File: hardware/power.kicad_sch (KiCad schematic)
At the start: 19 parts, among them U1 RY1303

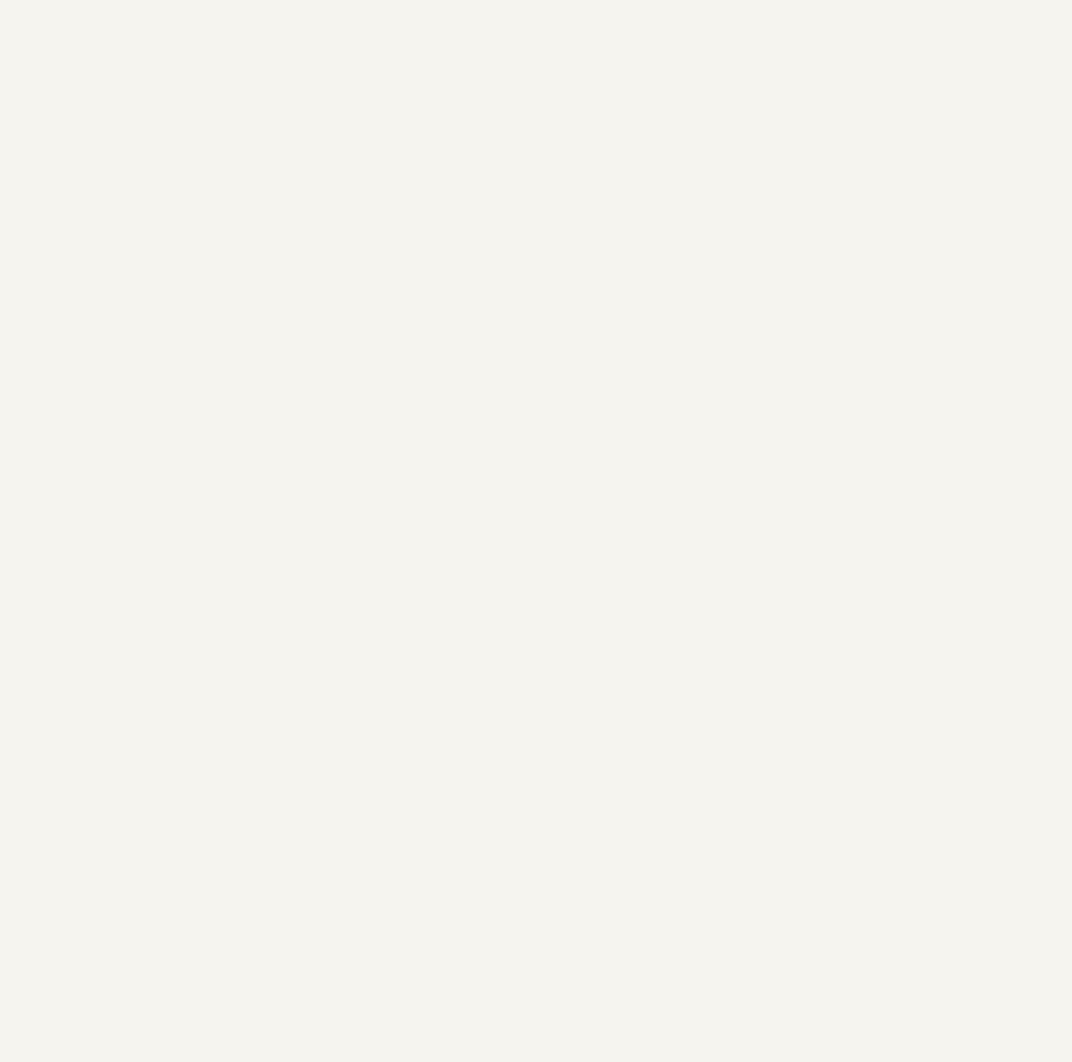
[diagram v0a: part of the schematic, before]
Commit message: 電源頁:兩顆 1.8V LDO 完成
U2/U3 皆用 KiCad 內建 Regulator_Linear:AP2112K-1.8,不必自建符號。
  U2  VIN→+3V3  EN→+3V3  VOUT→+1V8_SOC    Cin=C9   Cout=C11
  U3  VIN→+3V3  EN→+3V3  VOUT→+1V8_HDMI   Cin=C10  Cout=C12
兩顆同料號(011 §3),ADV7511 依 ADI §6.8 需專屬 LDO。

★ U3 一開始整顆接錯,其中兩項會燒件:
  VIN→GND(無輸入)、EN→GND(關閉)、VOUT→+1V8_SOC(接到 U2 的輸出)、C10 兩腳短路。
  第三項最危險:LDO 內部 VOUT→VIN 有寄生二極體(同概念 ⑦ 的 IO 箝位二極體),
  U2 的 1.8V 從 U3 的 VOUT 灌入而其 VIN=0V → 反向偏壓,
  U3 可能燒毀且會拉垮 U2 輸出。

★ 模式:「複製後漏改」連續第二次
  09-29 複製 buck 那路漏改 FB 接點;09-30 複製 LDO 那組漏改 VIN/EN/VOUT。
  兩次都「看起來完全正常」,只有 netlist 抓得到。
  對策定為流程:複製後立刻寫出這一組有幾處要改,逐項打勾再往下畫。

命名:+1V8_SoC → +1V8_SOC(小寫 o)。
  與前一天的 +3.3V/+3V3 同一個坑但只差大小寫,更難目視發現。
  驗證時加了大小寫衝突檢查(net 名轉大寫後找重複)。

三路 buck 回歸測試通過,未被改壞。

Co-Authored-By: Claude Opus 5 <noreply@anthropic.com>
Claude-Session: https://claude.ai/code/session_01HtGUWSQFey6W2g2grqgTMR
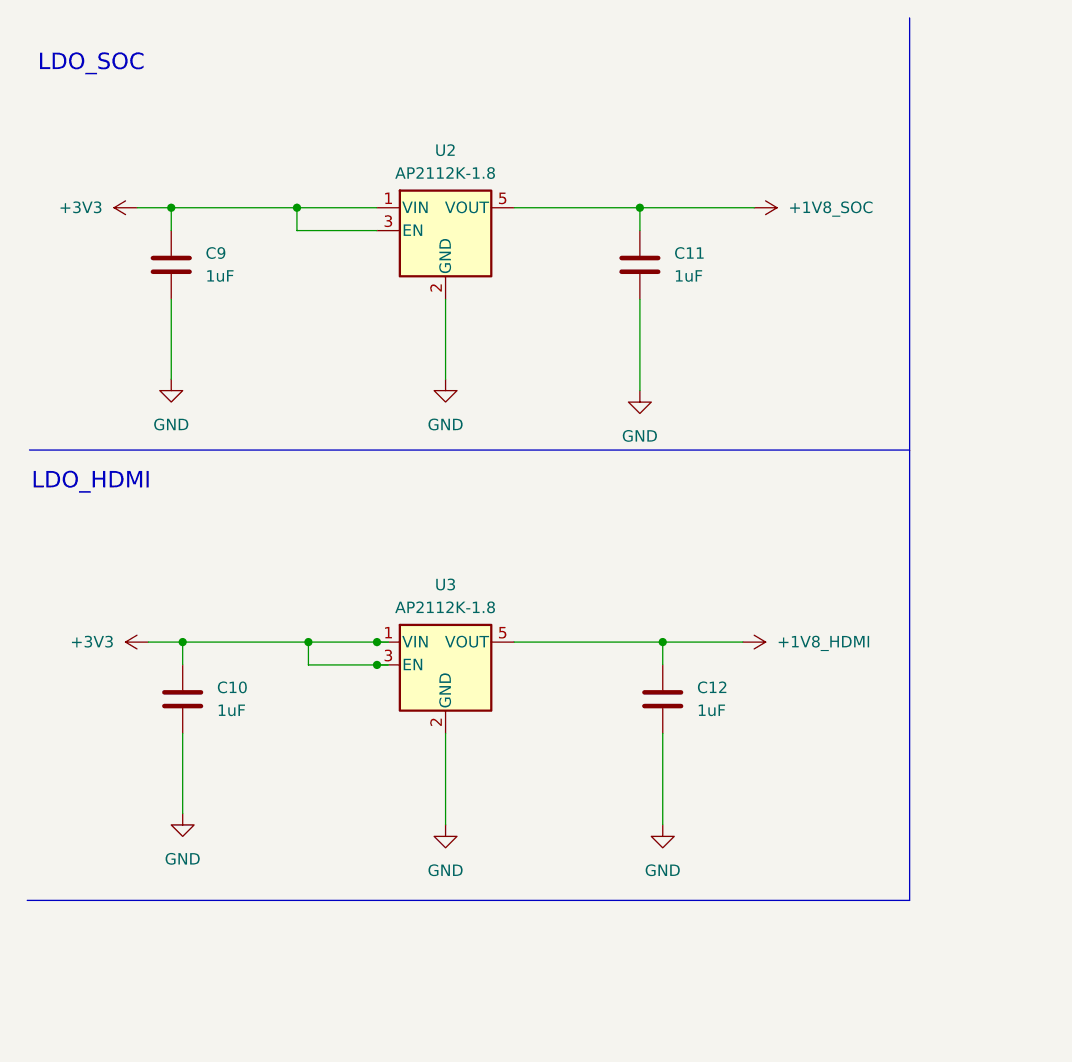
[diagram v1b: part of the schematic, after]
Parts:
- added C10, C9: 1uF, Package_TO_SOT_SMD:SOT-23-5, symbol Device:C
- added C11, C12: 1uF, symbol Device:C
- added U2, U3: AP2112K-1.8, Package_TO_SOT_SMD:SOT-23-5, symbol Regulator_Linear:AP2112K-1.8
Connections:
- net +3V3: now also C10.1, C9.1, U2.1 (VIN), U2.3 (EN), U3.1 (VIN), U3.3 (EN)
- net GND: now also C10.2, C11.2, C12.2, C9.2, U2.2 (GND), U3.2 (GND)
- new net +1V8_HDMI: C12.1, U3.5 (VOUT)
- new net +1V8_SOC: C11.1, U2.5 (VOUT)
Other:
- note added: "LDO_HDMI"
- note added: "LDO_SOC"

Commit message: RY1303 完成:VCC 接上 +5V_VBUS,21 腳全數接好
繞過「從庫更新符號」的做法:
  該動作的 Reset Fields 勾選項會把圖上 22 個被動件的 Value
  覆寫成庫預設值 C / R / L(接線完好但值全失)。
  改為直接修改 .kicad_sch 內 lib_symbols 快取中 RY1303 的 pin 16
  (no_connect/NC → power_in/VCC),KiCad 開檔即用這份快取,
  完全不需執行那個會清值的更新動作。

值損壞先以 git checkout 364ab9a -- hardware/power.kicad_sch 還原
(22 個值全部回來),再套用快取修改。

驗證:
  U1 21 支腳全部接好,pin 16 → +5V_VBUS
  C13 0.1uF 去耦 +5V_VBUS/GND
  22 個元件值全部保留
  三路 buck 回歸通過、兩顆 LDO 完好、無孤立 net

devlog 記三條教訓:
  ① 改符號名稱/型別安全,改位置/邊/索引會炸掉連線
  ② 更新符號對話框有「重設/reset/覆寫」字樣的一律不勾
  ③ 只改符號定義本身時,直接改 lib_symbols 快取比走更新流程安全
     (僅限不改幾何的情況)

Co-Authored-By: Claude Opus 5 <noreply@anthropic.com>
Claude-Session: https://claude.ai/code/session_01HtGUWSQFey6W2g2grqgTMR
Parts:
- added C13: 0.1uF, symbol Device:C
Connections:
- net +5V_VBUS: now also U1.16 (VCC), C13.1
- net GND: now also C13.2
- no-connect marks 1 -> 0

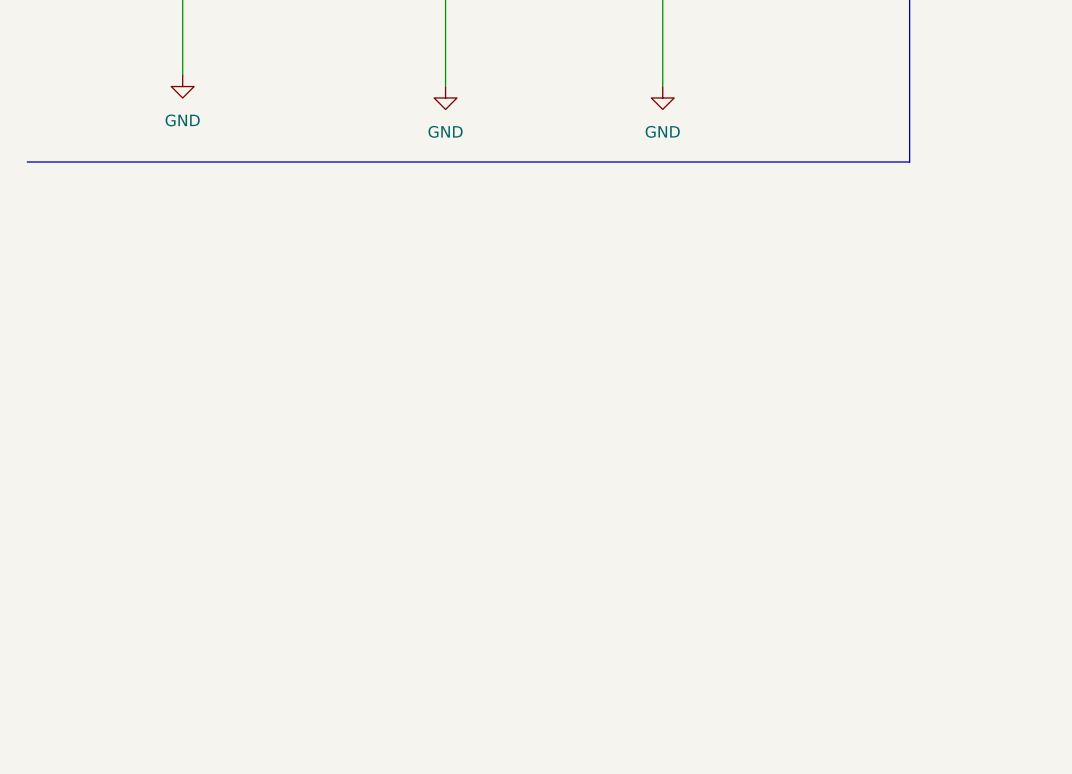
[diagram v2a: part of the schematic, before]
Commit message: 電源頁:RESET supervisor 完成;定下訊號 net 命名規則
U4 APX803-29SAG-7  VCC→+3V3  GND→GND  RESET#→SYS_RESET_N
R8 10K             SYS_RESET_N → +1V8_SOC

★ 上拉軌是這段最容易錯的:T113 的 RESET 是 1.8V 域輸入,
  而 APX803 是 open-drain —— 只負責拉低,高電位由上拉那端決定,
  所以 VCC 吃 3.3V、輸出擺到 1.8V 是正常且必要的。

第一次用全域標籤(SYS_RESET_N,電源頁 → 主晶片頁 T113 pin27)。
電源符號有 ERC 驅動源檢查,全域標籤沒有 —— 用途不同。

★ 訊號 net 命名規則(因應已踩過兩次的命名坑):
  低有效用 _N 結尾,不用 ~{NAME} 或 NAME#(匯出時特殊字元易出事)
  全大寫、底線分隔
  符號 pin 名稱可用 ~{RESET}(顯示上橫線),net 名稱用純 ASCII,兩者不必相同

順手更正 §4.3 時序驗算:EN1 閾值 1.2V→2V 後
  t 4.7ms → 9.6ms,T2 195ms → 190ms,仍 > 64ms 餘裕近 3 倍

現況:28 元件、15 net、無孤立、值全填,三路 buck 回歸通過

Co-Authored-By: Claude Opus 5 <noreply@anthropic.com>
Claude-Session: https://claude.ai/code/session_01HtGUWSQFey6W2g2grqgTMR
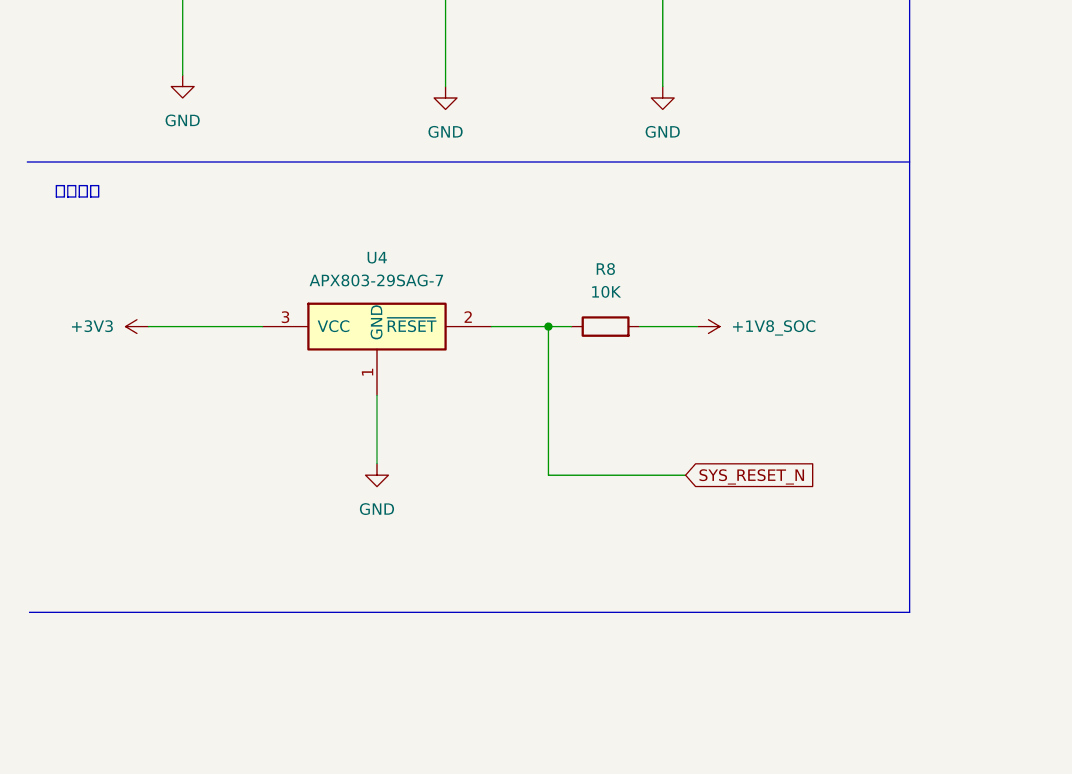
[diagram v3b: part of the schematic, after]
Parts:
- added R8: 10K, Resistor_SMD:R_0603_1608Metric, symbol Device:R
- added U4: APX803-29SAG-7, Package_TO_SOT_SMD:SOT-23, symbol T113-DEV-V1-power:APX803-29SA
- C13: footprint (none) -> Capacitor_SMD:C_0603_1608Metric
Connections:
- net +1V8_SOC: now also R8.2
- net +3V3: now also U4.3 (VCC)
- net GND: now also U4.1 (GND)
- new net SYS_RESET_N: R8.1, U4.2 (~{RESET})
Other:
- note added: "監測電源"

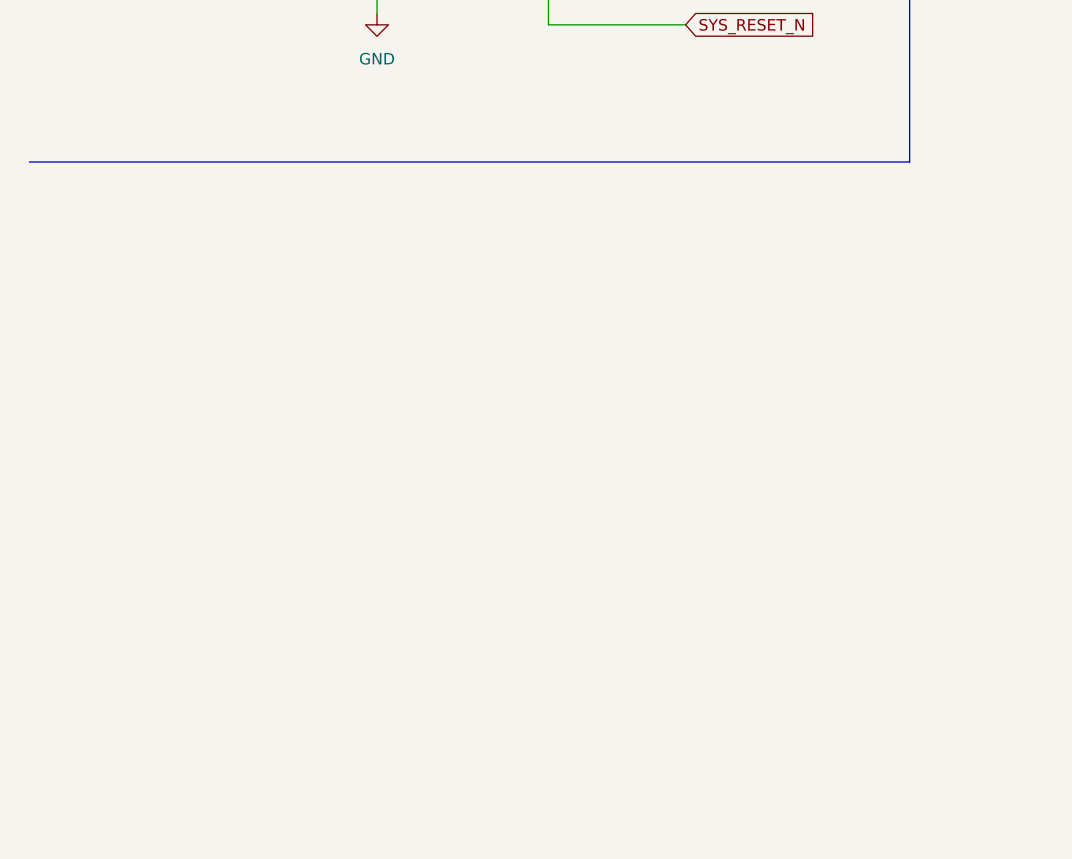
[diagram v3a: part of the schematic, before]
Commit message: ★ 電源頁完成:TPS2051B USB-A 限流接完
U5 TPS2051BDBVR
  pin5 IN  ← +5V_VBUS      pin1 OUT → +5V_USB
  pin4 EN  ← USB_EN(全域標籤,高有效)
  pin3 OC# → USB_OC_N + R9 10K 上拉到 +3V3(open-drain)
  pin2 GND ← GND
  C14 220uF SMD 電解 + C15 0.1uF  掛在 +5V_USB

過程中踩到第四次命名坑:pin5 一開始接到自建的「+5V」
(只有 1 個連接點的孤立 net),而圖上其他地方是「+5V_VBUS」——
電氣意圖正確但名字不同 = 沒真的連上。已修正。

C14 選 220uF 的依據(011 §6.3 補完整):
  USB 2.0 §7.2.4.1 要求 downstream port bulk ≥120uF
  (最壞情況:滿載 500mA 裝置突然插入時要撐住 VBUS)
  220uF 是最接近且超過規範的標準值,與 47uF 價差不到幾分錢。
  並聯 0.1uF 因電解 ESL 高、高頻已不像電容(概念 ⑧ 的 SRF)。
  這是全板唯一的電解、也是 0603 統一規則的唯一例外,已標註在 012 §4.1.1。

check_power_rails.py 加入跨頁訊號白名單 ——
USB_EN / USB_OC_N / SYS_RESET_N 在對手方那頁畫好之前只有一個連接點,
那不是錯,改為列在「跨頁訊號(非錯誤)」區並附等待對象。

電源頁現況:32 元件、18 條 net、值全填、無命名衝突、三路 buck 通過。
待補:元件 Footprint/LCSC 欄位、U5 的 IN 側 0.1uF、跑一次 ERC。

Co-Authored-By: Claude Opus 5 <noreply@anthropic.com>
Claude-Session: https://claude.ai/code/session_01HtGUWSQFey6W2g2grqgTMR
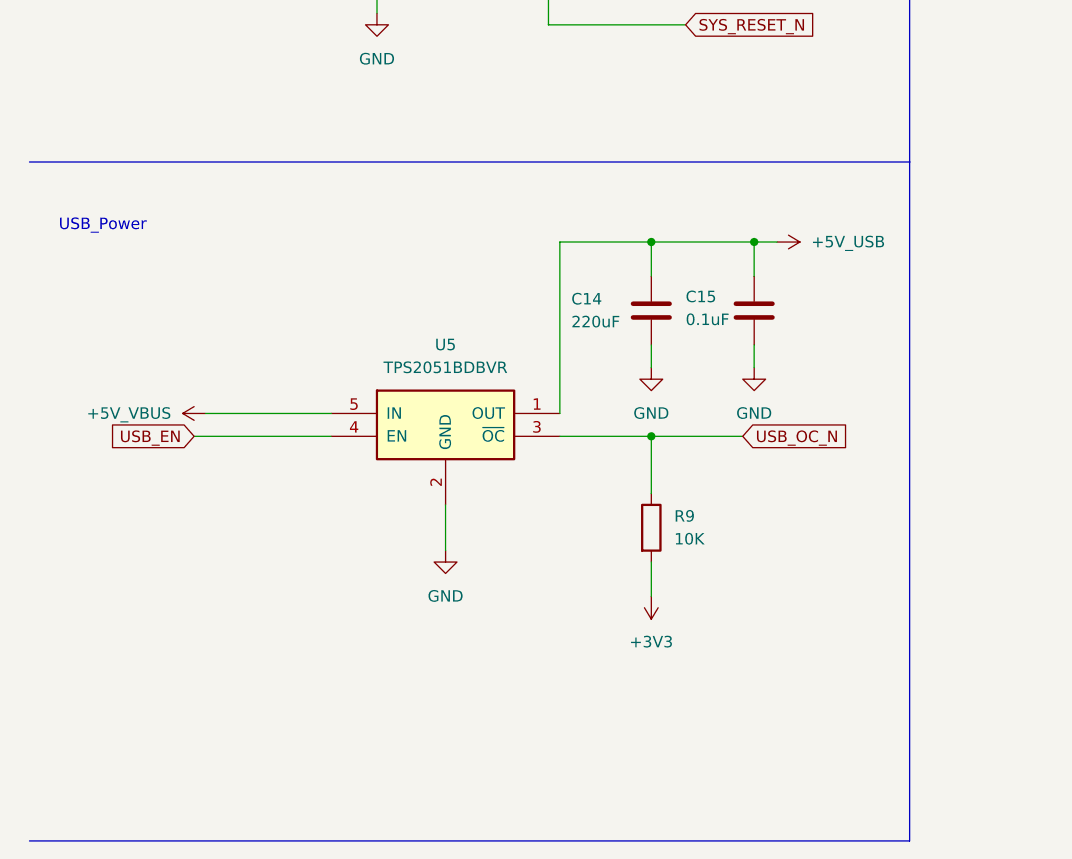
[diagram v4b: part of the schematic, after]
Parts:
- added C14: 220uF, symbol Device:C
- added C15: 0.1uF, symbol Device:C
- added R9: 10K, Package_TO_SOT_SMD:SOT-23, symbol Device:R
- added U5: TPS2051BDBVR, Package_TO_SOT_SMD:SOT-23-5, symbol T113-DEV-V1-power:TPS2051B
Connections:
- net +3V3: now also R9.2
- net +5V_VBUS: now also U5.5 (IN)
- net GND: now also C14.2, C15.2, U5.2 (GND)
- new net +5V_USB: C14.1, C15.1, U5.1 (OUT)
- new net USB_EN: U5.4 (EN)
- new net USB_OC_N: R9.1, U5.3 (~{OC})
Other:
- note added: "USB_Power"
